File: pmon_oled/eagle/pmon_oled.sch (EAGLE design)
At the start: 44 parts, among them J1 USB, J2 USB, J3 PINHD-1X3, J4 PINHD-2X3, J5 PINHD-1X3, Q1 16Mhz, U1 LTC2943, U2 FT232RL, U3 LT1764AEQ, U4 ATMEGA328TQFP32

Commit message: Checkin in pending changes.
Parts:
- removed D2, D3: GREEN, pmon_uno:LED1206
- removed D5: BLUE, pmon_uno:LED1206
- removed R10, R11, R13: 3K3, pmon_uno:RES-R0603
- added J6: JUMPER_SOLDER_1X2, dp_devices:JUMPER_SOLDER_1X2
- added R14, R15: 10K, pmon_uno:RES-R0603
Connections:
- removed net ACTIVITY_LED: R10.2, U4.PB1(OC1A)
- removed net N$14: D5.A, R13.2
- removed net N$20: D3.A, R11.1
- removed net N$3: D2.A, R10.1
- removed net STATUS_LED: R11.2, U4.PD3(INT1)
- removed net V+: C6.+, C9.1, R13.1, R4.I2, U3.OUT
- new net N$12: C7.2, J6.1
- new net N$6: R14.2, U2.TXO
- new net N$8: R15.2, U2.RXI
- new net VUSB: C3.+, C5.1, J2.VBUS, J5.1, U2.VCC, U2.VCCIO
- net +5V: now also C1.+, C4.1, J5.2, U3.IN, U3.SHDN; no longer C3.+, C5.1, J2.VBUS, J5.1, U2.VCC, U2.VCCIO
- net GND: no longer D2.C, D3.C, D5.C
- net N$9: now also C6.+, C9.1, R4.I2, U3.OUT; no longer C1.+, C4.1, J5.2, U3.IN, U3.SHDN
- net RESET: now also J6.2; no longer C7.2
- net SER_RX: now also R14.1; no longer U2.TXO
- net SER_TX: now also R15.1; no longer U2.RXI
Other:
- note added: "*"
- note added: "+5V"
- note added: "Power Play - OLED"
- note added: "SENSE"
- note added: "SOURCE"
- note added: "USB"
- note removed: "Arduino Single Cell Battery Power Monitor"
- note removed: "C/V/A SENSE"
- note removed: "DIAGNOSTICS"
- note removed: "FROM CHARGER"
- note removed: "POWER SELECTOR"
- note removed: "TO COMPUTER"
- moved on the sheet: C1, C3, C4, C5, C6, C7, C8, C9, D1, D4, J1, J2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

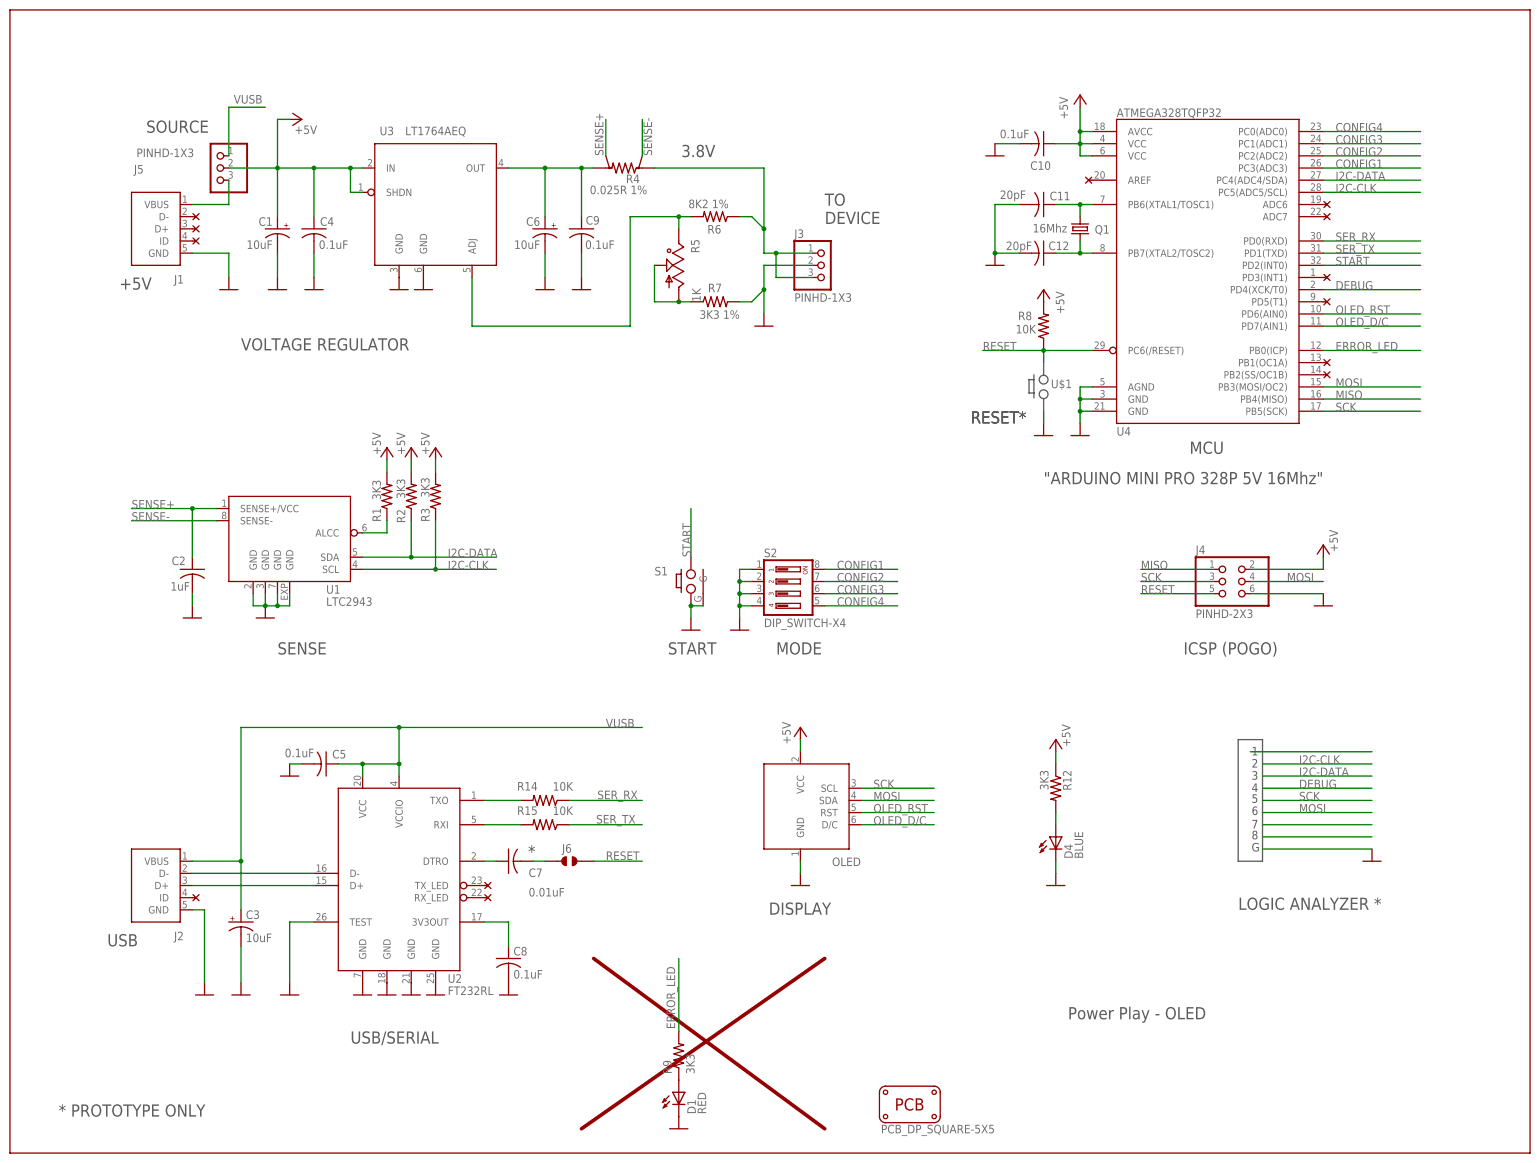
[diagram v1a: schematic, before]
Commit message: Routed critical networks. Ready for final auto routing.
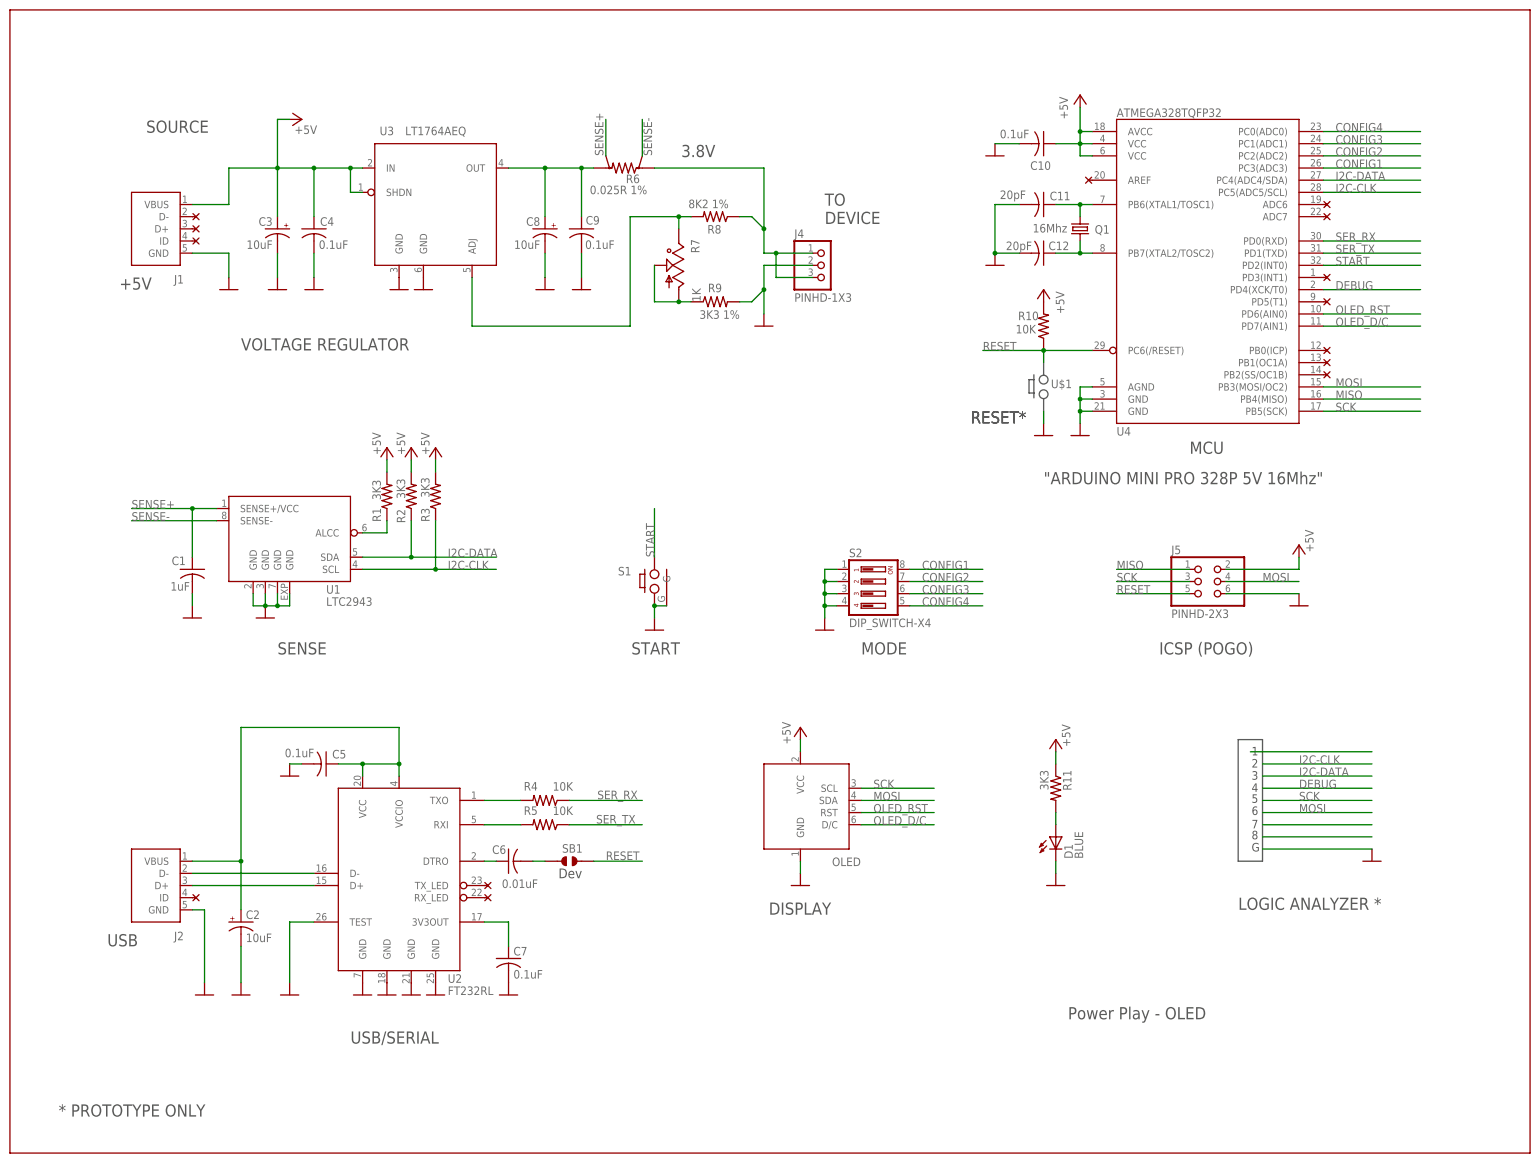
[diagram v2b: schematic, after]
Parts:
- removed D4: BLUE, pmon_uno:LED1206
- removed J3: PINHD-1X3, pmon_uno:PINHD-1X3
- removed J6: JUMPER_SOLDER_1X2, dp_devices:JUMPER_SOLDER_1X2
- removed PCB1: PCB_DP_SQUARE-5X5, pmon_uno:PCB_DP_SQUARE-5X5
- removed R12: 3K3, pmon_uno:RES-R0603
- removed R14, R15: 10K, pmon_uno:RES-R0603
- added R10: 10K, pmon_oled:RES-R0603
- added R11: 3K3, pmon_oled:RES-R0603
- added SB1: JUMPER_SOLDER_1X2, pmon_oled:JUMPER_SOLDER_1X2
- C1: value 10uF -> 1uF; device pmon_uno:CPOL-USA/3216-18R -> pmon_oled:CAP-C0603
- C10, C11, C12, C4, C5, C9: device pmon_uno:CAP-C0603 -> pmon_oled:CAP-C0603
- C2: value 1uF -> 10uF; device pmon_uno:CAP-C0603 -> pmon_oled:CPOL-USA/3216-18R
- C3: device pmon_uno:CPOL-USA/3216-18R -> pmon_oled:CPOL-USA/3216-18R
- C6: value 10uF -> 0.01uF; device pmon_uno:CPOL-USA/3216-18R -> pmon_oled:CAP-C0603
- C7: value 0.01uF -> 0.1uF; device pmon_uno:CAP-C0603 -> pmon_oled:CAP-C0603
- C8: value 0.1uF -> 10uF; device pmon_uno:CAP-C0603 -> pmon_oled:CPOL-USA/3216-18R
- D1: value RED -> BLUE; device pmon_uno:LED1206 -> pmon_oled:LED1206
- J1, J2: device pmon_uno:USB -> pmon_oled:USB
- J4: value PINHD-2X3 -> PINHD-1X3; device pmon_uno:PINHD-2X3 -> pmon_oled:PINHD-1X3
- J5: value PINHD-1X3 -> PINHD-2X3; device pmon_uno:PINHD-1X3 -> pmon_oled:PINHD-2X3
- Q1: device pmon_uno:CRYSTALCTS406 -> pmon_oled:CRYSTALCTS406
- R1, R2, R3: device pmon_uno:RES-R0603 -> pmon_oled:RES-R0603
- R4: value 0.025R 1% -> 10K; device pmon_uno:RES-SHUNT-6432 -> pmon_oled:RES-R0603
- R5: value 1K -> 10K; device pmon_uno:TRIM_US-SM-42/43A -> pmon_oled:RES-R0603
- R6: value 8K2 1% -> 0.025R 1%; device pmon_uno:RES-R0603 -> pmon_oled:RES-SHUNT-6432
- R7: value 3K3 1% -> 1K; device pmon_uno:RES-R0603 -> pmon_oled:TRIM_US-SM-42/43A
- R8: value 10K -> 8K2 1%; device pmon_uno:RES-R0603 -> pmon_oled:RES-R0603
- R9: value 3K3 -> 3K3 1%; device pmon_uno:RES-R0603 -> pmon_oled:RES-R0603
- S1: device pmon_uno:PUSH_BUTTON_SHIELDED -> pmon_oled:PUSH_BUTTON_SHIELDED
- S2: device pmon_uno:DIP_SWITCH-X4 -> pmon_oled:DIP_SWITCH-X4
- U1: device pmon_uno:LTC2943 -> pmon_oled:LTC2943
- U2: device pmon_uno:FT232RL -> pmon_oled:FT232RL
- U3: device pmon_uno:LTE1764 -> pmon_oled:LTE1764
- U4: device pmon_uno:ATMEGA328TQFP32 -> pmon_oled:ATMEGA328TQFP32
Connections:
- removed net ERROR_LED: R9.2, U4.PB0(ICP)
- removed net N$4: D1.A, R9.1
- removed net N$5: J1.VBUS, J5.3
- net +5V: now also C3.+, J1.VBUS, R10.2, R11.1; no longer C1.+, J4.2, R12.1, R8.2
- net GND: now also C1.2, C2.-, C7.2, C8.-, J4.2, J5.6, R9.2; no longer C1.-, C2.2, C6.-, C8.2, D4.C, J3.2, J4.6, R7.2
- net MISO: now also J5.1; no longer J4.1
- net MOSI: now also J5.4; no longer J4.4
- net N$11: now also C6.1; no longer C7.1
- net N$12: now also C6.2, SB1.1; no longer C7.2, J6.1
- net N$16: now also C7.1; no longer C8.1
- net N$17: now also D1.A, R11.2; no longer D4.A, R12.2
- net N$18: now also R7.2, R9.1; no longer R5.1, R5.2
- net N$19: now also R7.3, R8.2; no longer R5.3, R6.2
- net N$22: now also J4.1, J4.3, R6.I1, R8.1; no longer J3.1, J3.3, R4.I1, R6.1
- net N$6: now also R4.2; no longer R14.2
- net N$8: now also R5.2; no longer R15.2
- net N$9: now also C8.+, R6.I2; no longer C6.+, R4.I2
- net RESET: now also J5.5, R10.1, SB1.2; no longer J4.5, J6.2, R8.1
- net SCK: now also J5.3; no longer J4.3
- net SENSE+: now also C1.1, R6.V2; no longer C2.1, R4.V2
- net SENSE-: now also R6.V1; no longer R4.V1
- net SER_RX: now also R4.1; no longer R14.1
- net SER_TX: now also R5.1; no longer R15.1
- net VUSB: now also C2.+; no longer C3.+, J5.1
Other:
- note added: "Dev"
- note removed: "*"
- moved on the sheet: C3, C7, D1, R8, R9, S1, S2

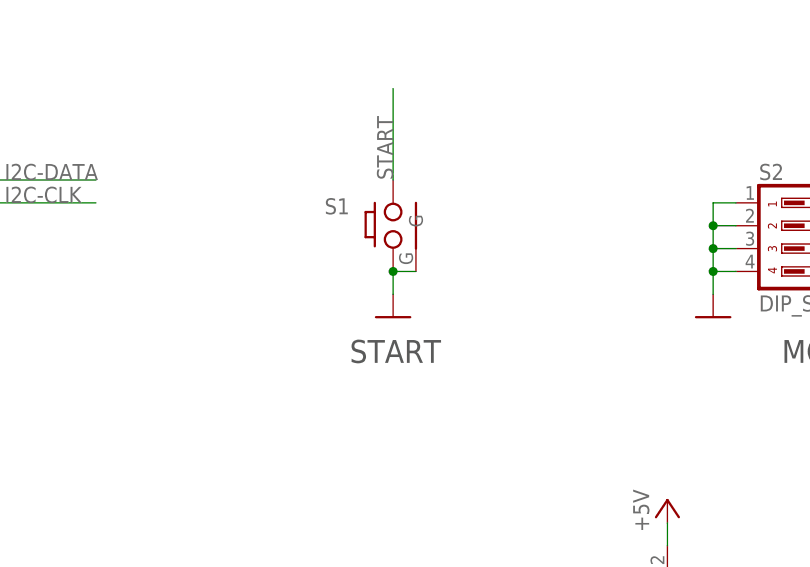
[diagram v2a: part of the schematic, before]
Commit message: Updated the layout for physical clearance.
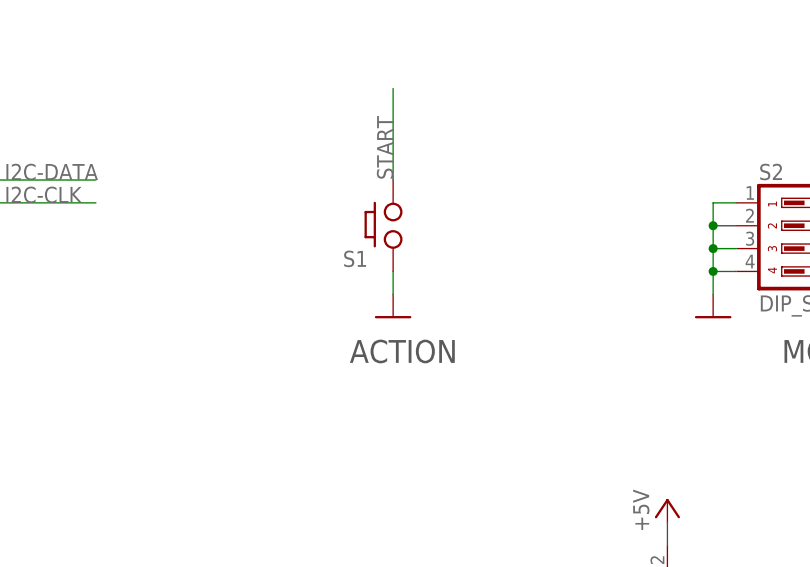
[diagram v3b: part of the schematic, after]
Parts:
- S1: value PUSH_BUTTON_SHIELDED -> PUSH_BUTTON; device pmon_oled:PUSH_BUTTON_SHIELDED -> pmon_oled:PUSH_BUTTON
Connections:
- net GND: no longer S1.G
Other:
- note added: "ACTION"
- note removed: "START"
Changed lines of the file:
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@@
 <part name="U$7" library="pmon_oled" deviceset="NC" device=""/>
 <part name="U$8" library="pmon_oled" deviceset="NC" device=""/>
-<part name="S1" library="pmon_oled" deviceset="PUSH_BUTTON_SHIELDED" device=""/>
 <part name="J4" library="pmon_oled" deviceset="PINHD-1X3" device="" value="PINHD-1X3"/>
 <part name="P+6" library="pmon_oled" deviceset="+5V" device=""/>
@@
 <part name="SB1" library="pmon_oled" deviceset="JUMPER_SOLDER_1X2" device=""/>
 <part name="U$14" library="pmon_oled" deviceset="NC" device=""/>
+<part name="S1" library="pmon_oled" deviceset="PUSH_BUTTON" device=""/>
 </parts>
 <sheets>
@@
 <text x="165.1" y="152.4" size="2.54" layer="97">RESET*</text>
 <text x="180.34" y="139.7" size="2.54" layer="97">"ARDUINO MINI PRO 328P 5V 16Mhz"</text>
-<text x="94.234" y="104.14" size="2.54" layer="97">START</text>
+<text x="94.234" y="104.14" size="2.54" layer="97">ACTION</text>
 <text x="-7.112" y="213.106" size="2.54" layer="97">SOURCE</text>
 <text x="122.936" y="49.784" size="2.54" layer="97">DISPLAY</text>
@@
 <instance part="U$7" gate="G$1" x="2.54" y="193.04" rot="R180"/>
 <instance part="U$8" gate="G$1" x="2.54" y="190.5" rot="R180"/>
-<instance part="S1" gate="G$1" x="99.06" y="119.38" smashed="yes">
-<attribute name="NAME" x="91.44" y="120.65" size="1.778" layer="95"/>
-</instance>
 <instance part="J4" gate="A" x="134.62" y="185.42"/>
 <instance part="P+6" gate="1" x="25.4" y="215.9" smashed="yes" rot="R270">
@@
 </instance>
 <instance part="U$14" gate="G$1" x="238.76" y="167.64" rot="R180"/>
+<instance part="S1" gate="G$1" x="99.06" y="119.38" smashed="yes">
+<attribute name="NAME" x="93.472" y="114.808" size="1.778" layer="95"/>
+</instance>
 </instances>
 <busses>
@@
 <wire x1="99.06" y1="111.76" x2="99.06" y2="114.3" width="0.1524" layer="91"/>
 <pinref part="S1" gate="G$1" pin="1"/>
-<pinref part="S1" gate="G$1" pin="G"/>
-<wire x1="101.6" y1="114.3" x2="99.06" y2="114.3" width="0.1524" layer="91"/>
-<junction x="99.06" y="114.3"/>
-</segment>
-<segment>
+</segment>
+<segment>

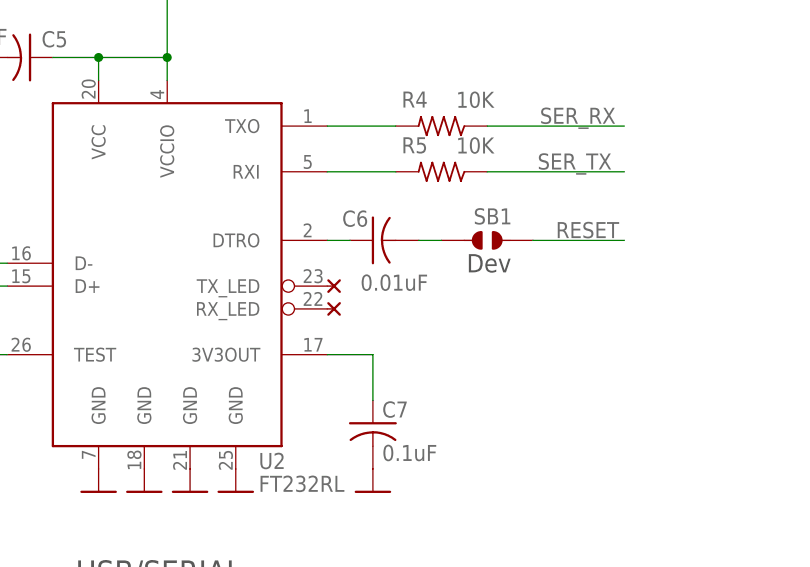
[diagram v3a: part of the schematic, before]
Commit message: Changed reset capacitor from 0.01 to 0.1 (to reduce compoent kind count).
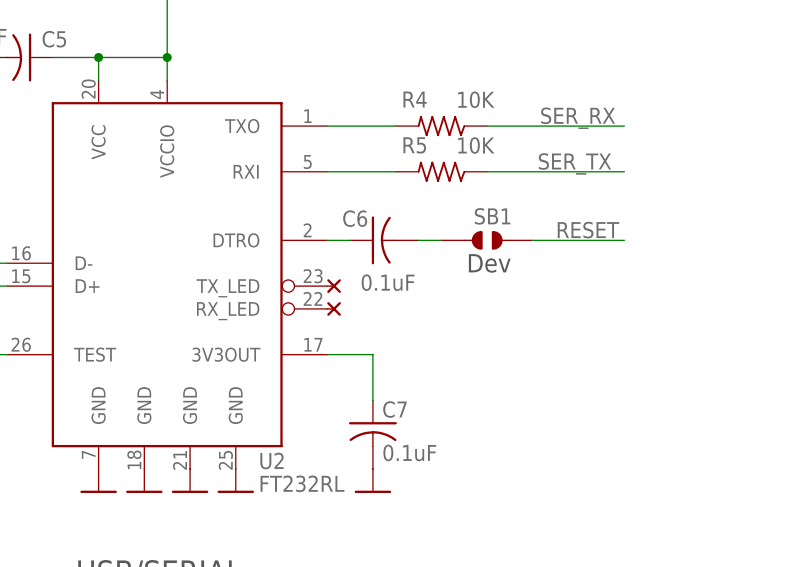
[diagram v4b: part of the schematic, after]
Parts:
- C6: value 0.01uF -> 0.1uF
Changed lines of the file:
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@@
 </classes>
 <parts>
-<part name="C6" library="pmon_oled" deviceset="CAP-" device="C0603" value="0.01uF"/>
+<part name="C6" library="pmon_oled" deviceset="CAP-" device="C0603" value="0.1uF"/>
 <part name="P+2" library="pmon_oled" deviceset="+5V" device=""/>
 <part name="GND16" library="pmon_oled" deviceset="GND" device=""/>
